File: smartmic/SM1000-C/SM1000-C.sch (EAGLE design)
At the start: 199 parts, among them CN1 HDR100-3, CN10 MJ-3523-SMT, CN11 HDR100-3, CN12 DF11-16DS, CN2 MOLEX-MINI-B-SMT, CN3 RASM722PX, CN4 RJ-45, CN5 MJ-3523-SMT, CN6 SJ-3524, CN7 MJ-3523-SMT, CN8 SJ-3524, CN9 MJ-3523-SMT, J1 JMP-2PIN, J3 JMP-2PIN, J4 JMP-2PIN, P1 TPAD50, P10 TPAD50, P11 TPAD50, P12 TPAD50, P13 TPAD50, P14 TPAD50, P15 TPAD50, P16 TPAD50, P17 TPAD50, P18 TPAD50, P19 TPAD50, P2 TPAD50, P20 TPAD50, P3 TPAD50, P4 TPAD50, P5 TPAD50, P6 TPAD50, P7 TPAD50, P8 TPAD50, P9 TPAD50, SW1 SW-BOURNS-7914S, SW2 SW-BOURNS-7914S, SW3 DPDT, SW4 SW-BOURNS-7914S, SW5 SW-BOURNS-7914J, T1 SM-LP-5001, T2 SM-LP-5001, U1 STM32F405, U2 LD3985M33R, U3 STMPS2141, U4 EMIF02-USB03F2, U5 TPS54329E, U6 LMV341, U7 LMV341, U8 LM386M-1, U9 LMV341

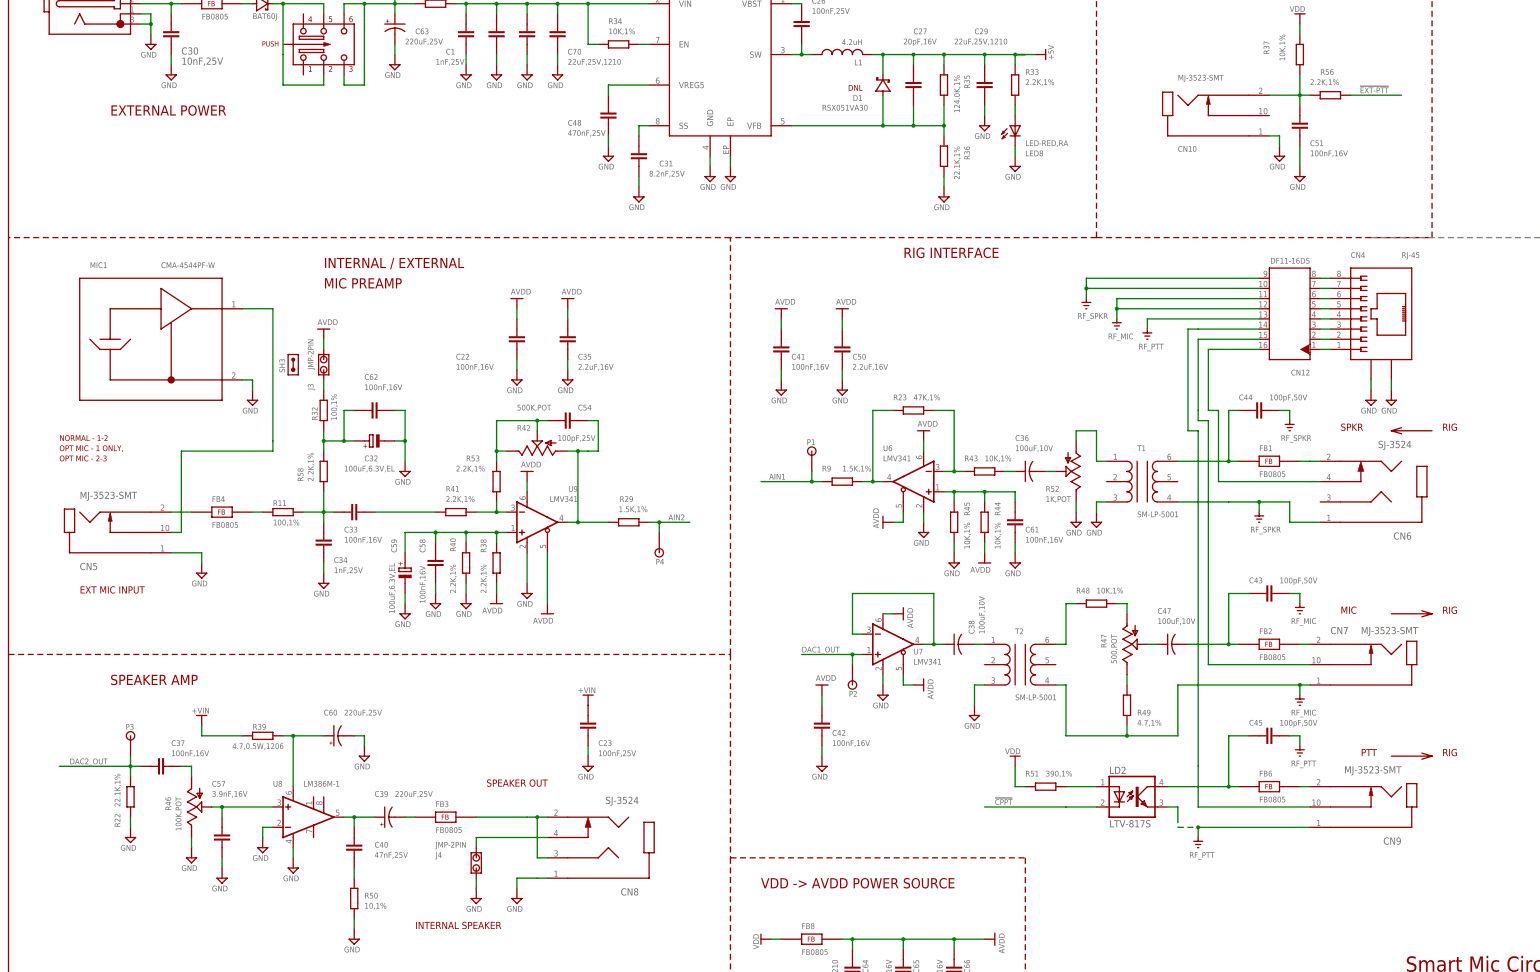
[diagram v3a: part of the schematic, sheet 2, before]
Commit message: Update Schemaatic, PCB & BOM to reflect change to 0402 package, Change 3.5mm conns to ST-3509 type RGB
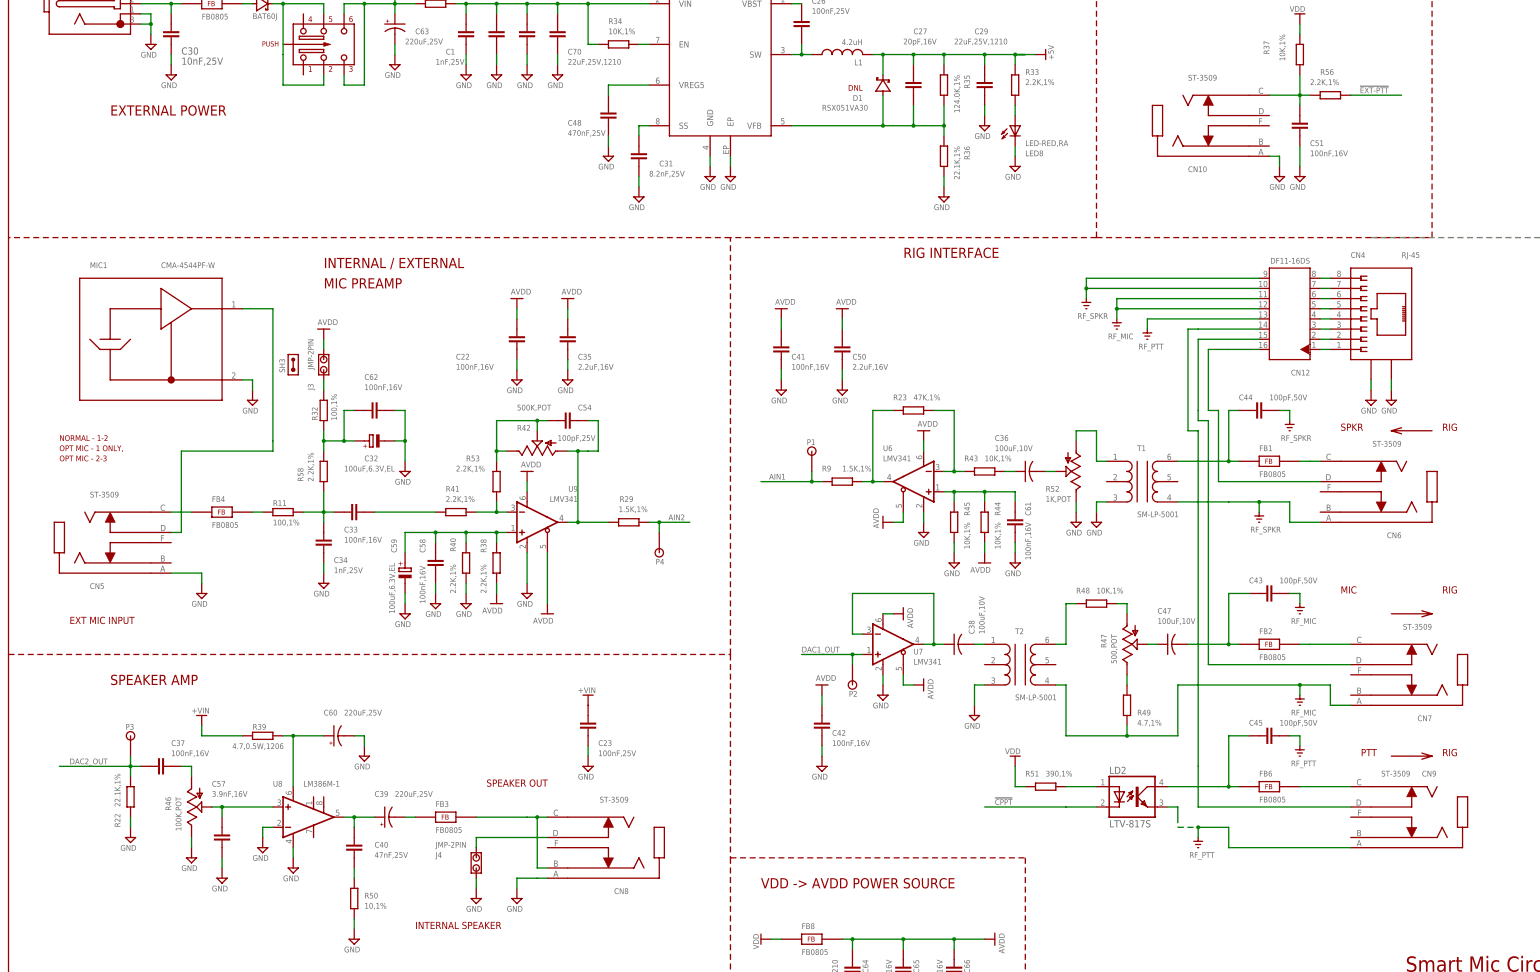
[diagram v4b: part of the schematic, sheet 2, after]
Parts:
- CN10, CN5, CN7, CN9: value MJ-3523-SMT -> ST-3509; device _RoweTel:MJ-3523-SMT -> _RoweTel:ST-3509
- CN6, CN8: value SJ-3524 -> ST-3509; device _RoweTel:SJ-3524 -> _RoweTel:ST-3509
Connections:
- removed net N$72: CN7.2, FB2.2
- new net N$70: CN7.C, FB2.2
- net APTT: now also CN9.D; no longer CN9.10
- net GND: now also CN5.A, CN8.A; no longer CN10.1, CN5.1, CN8.1
- net MIC: now also CN7.D; no longer CN7.10
- net N$15: now also CN10.C; no longer CN10.2
- net N$60: now also CN5.D; no longer CN5.10
- net N$62: now also CN8.D; no longer CN8.4
- net N$64: now also CN6.C; no longer CN6.2
- net N$73: now also CN9.C; no longer CN9.2
- net N$75: now also CN8.C; no longer CN8.2, CN8.3
- net N$76: now also CN5.C; no longer CN5.2
- net RF_MIC: now also CN7.A; no longer CN7.1
- net RF_PTT: now also CN9.A; no longer CN9.1
- net RF_SPKR: now also CN6.A; no longer CN6.1
- net SPKR: now also CN6.D; no longer CN6.4
